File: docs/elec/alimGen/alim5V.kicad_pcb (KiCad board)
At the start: 2 copper layers, 110 x 66 mm, 23 parts, among them P2 5V out, P3 MD49, P4 Charg, P5 Batt, P8 VOUTRegu, SW1 SW

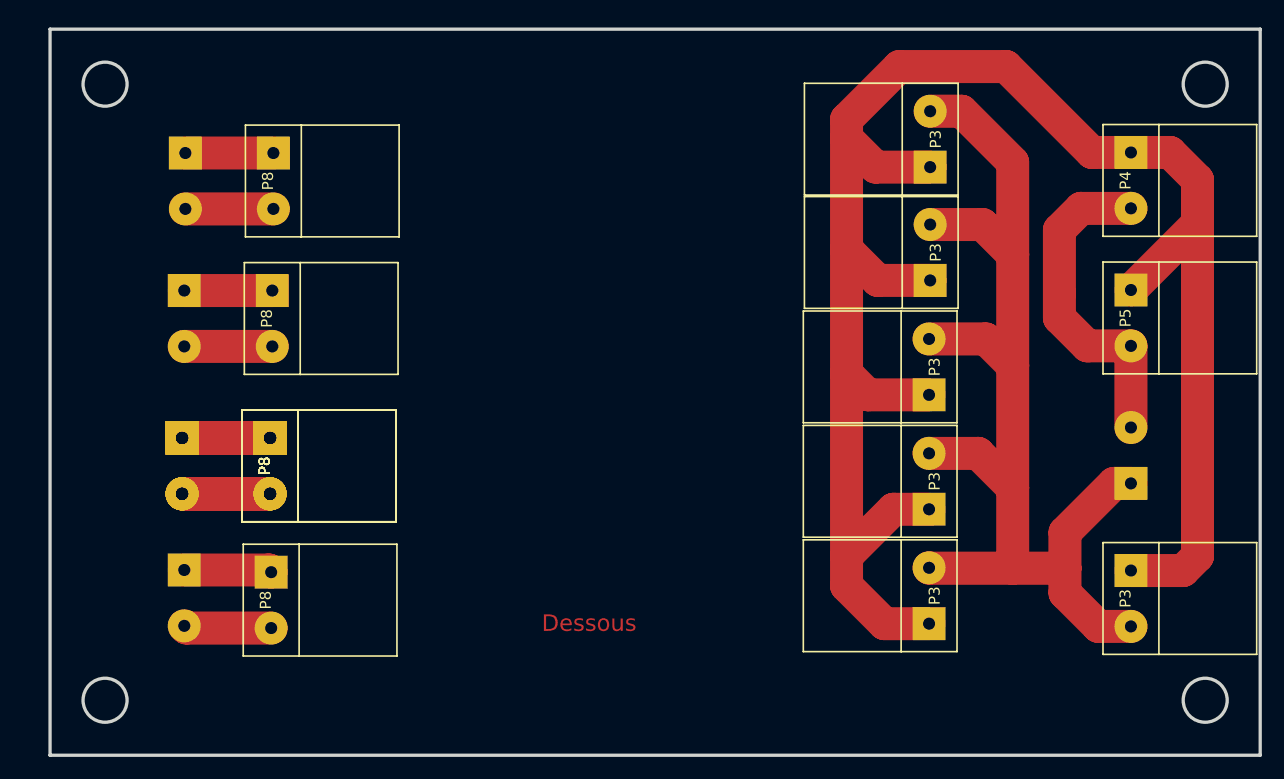
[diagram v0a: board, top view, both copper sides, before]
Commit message: docs réajustement du pcb de la carte alim
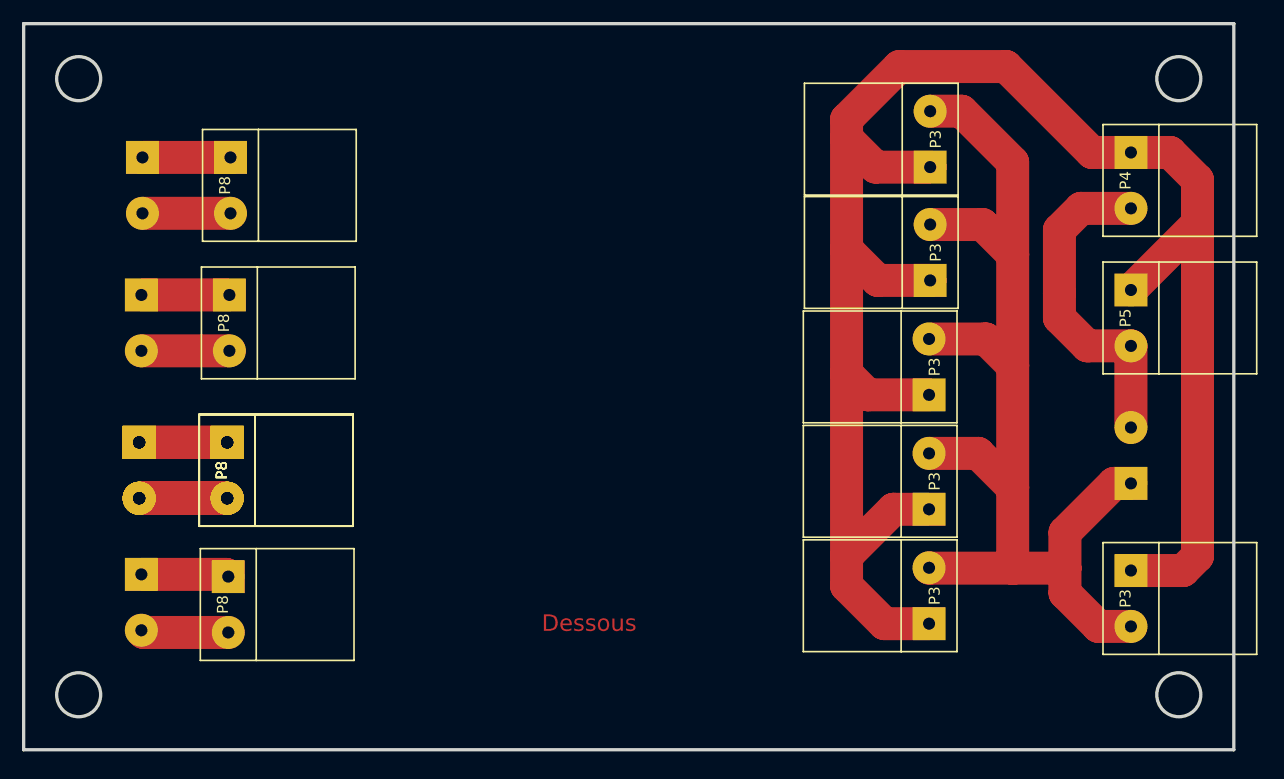
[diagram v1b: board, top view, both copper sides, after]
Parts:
- moved P8 3.92 mm to (32.3, 41.7)
- moved P2 3.92 mm to (24.4, 29.2)
- moved P2 3.92 mm to (24.3, 41.7)
- moved P2 3.92 mm to (24.1, 55.1) (x4)
- moved P8 3.92 mm to (32.1, 55.1) (x4)
- moved P8 3.92 mm to (32.4, 29.2)
- moved P2 3.92 mm to (24.3, 67.1)
- moved P8 3.92 mm to (32.2, 67.3)
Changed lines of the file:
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@@
     (links 41)
     (no_connects 6)
-    (area 15.599999 15.599999 126.555001 80.900001)
+    (area 11.794999 14.349999 126.555001 80.650001)
     (thickness 1.6)
     (drawings 9)
@@
     (pad_drill 0.762)
     (pad_to_mask_clearance 0.2)
-    (aux_axis_origin 16 81)
+    (aux_axis_origin 13.5 80.3)
     (visible_elements 7FFFFFFF)
     (pcbplotparams
@@
   )
   (module robair:Bornier5mm (layer B.Cu)
-    (at 28.2 66.7 270)
+    (at 24.3 67.1 270)
     (fp_text reference P2 (at 0 -0.5 270) (layer B.SilkS)
       (effects (font (size 1 1) (thickness 0.15)) (justify mirror))
@@
   )
   (module robair:Bornier5mm (layer F.Cu)
-    (at 36.1 66.9 270)
+    (at 32.2 67.3 270)
     (fp_text reference P8 (at 0 0.5 270) (layer F.SilkS)
       (effects (font (size 1 1) (thickness 0.15)))
@@
   )
   (module robair:Bornier5mm (layer B.Cu)
-    (at 28 54.7 270)
+    (at 24.1 55.1 270)
     (fp_text reference P2 (at 0 -0.5 270) (layer B.SilkS)
       (effects (font (size 1 1) (thickness 0.15)) (justify mirror))
@@
   )
   (module robair:Bornier5mm (layer F.Cu)
-    (at 36 54.7 270)
+    (at 32.1 55.1 270)
     (fp_text reference P8 (at 0 0.5 270) (layer F.SilkS)
       (effects (font (size 1 1) (thickness 0.15)))
@@
   )
   (module robair:Bornier5mm (layer F.Cu)
-    (at 36 54.7 270)
+    (at 32.1 55.1 270)
     (fp_text reference P8 (at 0 0.5 270) (layer F.SilkS)
       (effects (font (size 1 1) (thickness 0.15)))
@@
   )
   (module robair:Bornier5mm (layer B.Cu)
-    (at 28 54.7 270)
+    (at 24.1 55.1 270)
     (fp_text reference P2 (at 0 -0.5 270) (layer B.SilkS)
       (effects (font (size 1 1) (thickness 0.15)) (justify mirror))
@@
   )
   (module robair:Bornier5mm (layer B.Cu)
-    (at 28 54.7 270)
+    (at 24.1 55.1 270)
     (fp_text reference P2 (at 0 -0.5 270) (layer B.SilkS)
       (effects (font (size 1 1) (thickness 0.15)) (justify mirror))
@@
   )
   (module robair:Bornier5mm (layer F.Cu)
-    (at 36 54.7 270)
+    (at 32.1 55.1 270)
     (fp_text reference P8 (at 0 0.5 270) (layer F.SilkS)
       (effects (font (size 1 1) (thickness 0.15)))
@@
   )
   (module robair:Bornier5mm (layer F.Cu)
-    (at 36 54.7 270)
+    (at 32.1 55.1 270)
     (fp_text reference P8 (at 0 0.5 270) (layer F.SilkS)
       (effects (font (size 1 1) (thickness 0.15)))
@@
   )
   (module robair:Bornier5mm (layer F.Cu)
-    (at 36.2 41.3 270)
+    (at 32.3 41.7 270)
     (fp_text reference P8 (at 0 0.5 270) (layer F.SilkS)
       (effects (font (size 1 1) (thickness 0.15)))
@@
   )
   (module robair:Bornier5mm (layer B.Cu)
-    (at 28 54.7 270)
+    (at 24.1 55.1 270)
     (fp_text reference P2 (at 0 -0.5 270) (layer B.SilkS)
       (effects (font (size 1 1) (thickness 0.15)) (justify mirror))
@@
   )
   (module robair:Bornier5mm (layer B.Cu)
-    (at 28.2 41.3 270)
+    (at 24.3 41.7 270)
     (fp_text reference P2 (at 0 -0.5 270) (layer B.SilkS)
       (effects (font (size 1 1) (thickness 0.15)) (justify mirror))
@@
   )
   (module robair:Bornier5mm (layer B.Cu)
-    (at 28.3 28.8 270)
+    (at 24.4 29.2 270)
     (fp_text reference P2 (at 0 -0.5 270) (layer B.SilkS)
       (effects (font (size 1 1) (thickness 0.15)) (justify mirror))
@@
   )
   (module robair:Bornier5mm (layer F.Cu)
-    (at 36.3 28.8 270)
+    (at 32.4 29.2 270)
     (fp_text reference P8 (at 0 0.5 270) (layer F.SilkS)
       (effects (font (size 1 1) (thickness 0.15)))
@@
       (net 4 "Net-(P2-Pad2)"))
   )
-  (gr_circle (center 121 76) (end 121 78) (layer Edge.Cuts) (width 0.3))
-  (gr_circle (center 121 20) (end 123 20) (layer Edge.Cuts) (width 0.3))
-  (gr_circle (center 21 20) (end 19 20) (layer Edge.Cuts) (width 0.3))
-  (gr_circle (center 21 76) (end 19 76) (layer Edge.Cuts) (width 0.3))
-  (gr_line (start 126 15) (end 16 15) (angle 90) (layer Edge.Cuts) (width 0.3))
-  (gr_line (start 126 81) (end 126 15) (angle 90) (layer Edge.Cuts) (width 0.3))
-  (gr_line (start 16 81) (end 126 81) (angle 90) (layer Edge.Cuts) (width 0.3))
-  (gr_line (start 16 15) (end 16 81) (angle 90) (layer Edge.Cuts) (width 0.3))
+  (gr_circle (center 118.6 75.5) (end 118.6 77.5) (layer Edge.Cuts) (width 0.3))
+  (gr_circle (center 118.6 19.5) (end 120.6 19.5) (layer Edge.Cuts) (width 0.3))
+  (gr_circle (center 18.6 19.5) (end 16.6 19.5) (layer Edge.Cuts) (width 0.3))
+  (gr_circle (center 18.6 75.5) (end 16.6 75.5) (layer Edge.Cuts) (width 0.3))
+  (gr_line (start 123.6 14.5) (end 13.6 14.5) (angle 90) (layer Edge.Cuts) (width 0.3))
+  (gr_line (start 123.6 80.5) (end 123.6 14.5) (angle 90) (layer Edge.Cuts) (width 0.3))
+  (gr_line (start 13.6 80.5) (end 123.6 80.5) (angle 90) (layer Edge.Cuts) (width 0.3))
+  (gr_line (start 13.6 14.5) (end 13.6 80.5) (angle 90) (layer Edge.Cuts) (width 0.3))
   (gr_text Dessous (at 65 69) (layer F.Cu)
     (effects (font (size 1.5 1.5) (thickness 0.3)))
   )
-  (segment (start 28.2 64.16) (end 35.9 64.16) (width 3) (layer F.Cu) (net 1))
-  (segment (start 35.9 64.16) (end 36.1 64.36) (width 3) (layer F.Cu) (net 1))
-  (segment (start 36 52.16) (end 28 52.16) (width 3) (layer F.Cu) (net 1))
-  (segment (start 36 52.16) (end 28 52.16) (width 3) (layer F.Cu) (net 1))
-  (segment (start 36 52.16) (end 28 52.16) (width 3) (layer F.Cu) (net 1))
-  (segment (start 36 52.16) (end 28 52.16) (width 3) (layer F.Cu) (net 1))
-  (segment (start 28.2 38.76) (end 36.2 38.76) (width 3) (layer F.Cu) (net 1))
-  (segment (start 28.3 26.26) (end 36.3 26.26) (width 3) (layer F.Cu) (net 1))
+  (segment (start 24.3 64.56) (end 32 64.56) (width 3) (layer F.Cu) (net 1))
+  (segment (start 32 64.56) (end 32.2 64.76) (width 3) (layer F.Cu) (net 1))
+  (segment (start 32.1 52.56) (end 24.1 52.56) (width 3) (layer F.Cu) (net 1))
+  (segment (start 32.1 52.56) (end 24.1 52.56) (width 3) (layer F.Cu) (net 1))
+  (segment (start 32.1 52.56) (end 24.1 52.56) (width 3) (layer F.Cu) (net 1))
+  (segment (start 32.1 52.56) (end 24.1 52.56) (width 3) (layer F.Cu) (net 1))
+  (segment (start 24.3 39.16) (end 32.3 39.16) (width 3) (layer F.Cu) (net 1))
+  (segment (start 24.4 26.66) (end 32.4 26.66) (width 3) (layer F.Cu) (net 1))
   (segment (start 96 27.54) (end 91.04 27.54) (width 3) (layer F.Cu) (net 2))
   (segment (start 91.04 27.54) (end 88.4 24.9) (width 3) (layer F.Cu) (net 2))
@@
   (segment (start 107.75 39) (end 107.75 41.25) (width 3) (layer F.Cu) (net 3))
   (segment (start 109.71 31.29) (end 107.75 33.25) (width 3) (layer F.Cu) (net 3))
-  (segment (start 36.1 69.44) (end 28.4 69.44) (width 3) (layer F.Cu) (net 4))
-  (segment (start 28.4 69.44) (end 28.2 69.24) (width 3) (layer F.Cu) (net 4))
-  (segment (start 36 57.24) (end 28 57.24) (width 3) (layer F.Cu) (net 4))
-  (segment (start 36 57.24) (end 28 57.24) (width 3) (layer F.Cu) (net 4))
-  (segment (start 36 57.24) (end 28 57.24) (width 3) (layer F.Cu) (net 4))
-  (segment (start 36 57.24) (end 28 57.24) (width 3) (layer F.Cu) (net 4))
-  (segment (start 28.2 43.84) (end 36.2 43.84) (width 3) (layer F.Cu) (net 4))
-  (segment (start 36.3 31.34) (end 28.3 31.34) (width 3) (layer F.Cu) (net 4))
+  (segment (start 32.2 69.84) (end 24.5 69.84) (width 3) (layer F.Cu) (net 4))
+  (segment (start 24.5 69.84) (end 24.3 69.64) (width 3) (layer F.Cu) (net 4))
+  (segment (start 32.1 57.64) (end 24.1 57.64) (width 3) (layer F.Cu) (net 4))
+  (segment (start 32.1 57.64) (end 24.1 57.64) (width 3) (layer F.Cu) (net 4))
+  (segment (start 32.1 57.64) (end 24.1 57.64) (width 3) (layer F.Cu) (net 4))
+  (segment (start 32.1 57.64) (end 24.1 57.64) (width 3) (layer F.Cu) (net 4))
+  (segment (start 24.3 44.24) (end 32.3 44.24) (width 3) (layer F.Cu) (net 4))
+  (segment (start 32.4 31.74) (end 24.4 31.74) (width 3) (layer F.Cu) (net 4))
   (segment (start 95.9 53.56) (end 100.36 53.56) (width 3) (layer F.Cu) (net 5))
   (segment (start 100.36 53.56) (end 103.5 56.7) (width 3) (layer F.Cu) (net 5))
